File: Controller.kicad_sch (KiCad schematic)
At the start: 39 parts, among them J1 USB4105-GF-A-060, J2 SWD, SW61 BOOTSEL, SW62 RESET, U1 RP2354A, U2 AP2112K-3.3TRG1, U3 USBLC6-2SC6, X1 12MHz

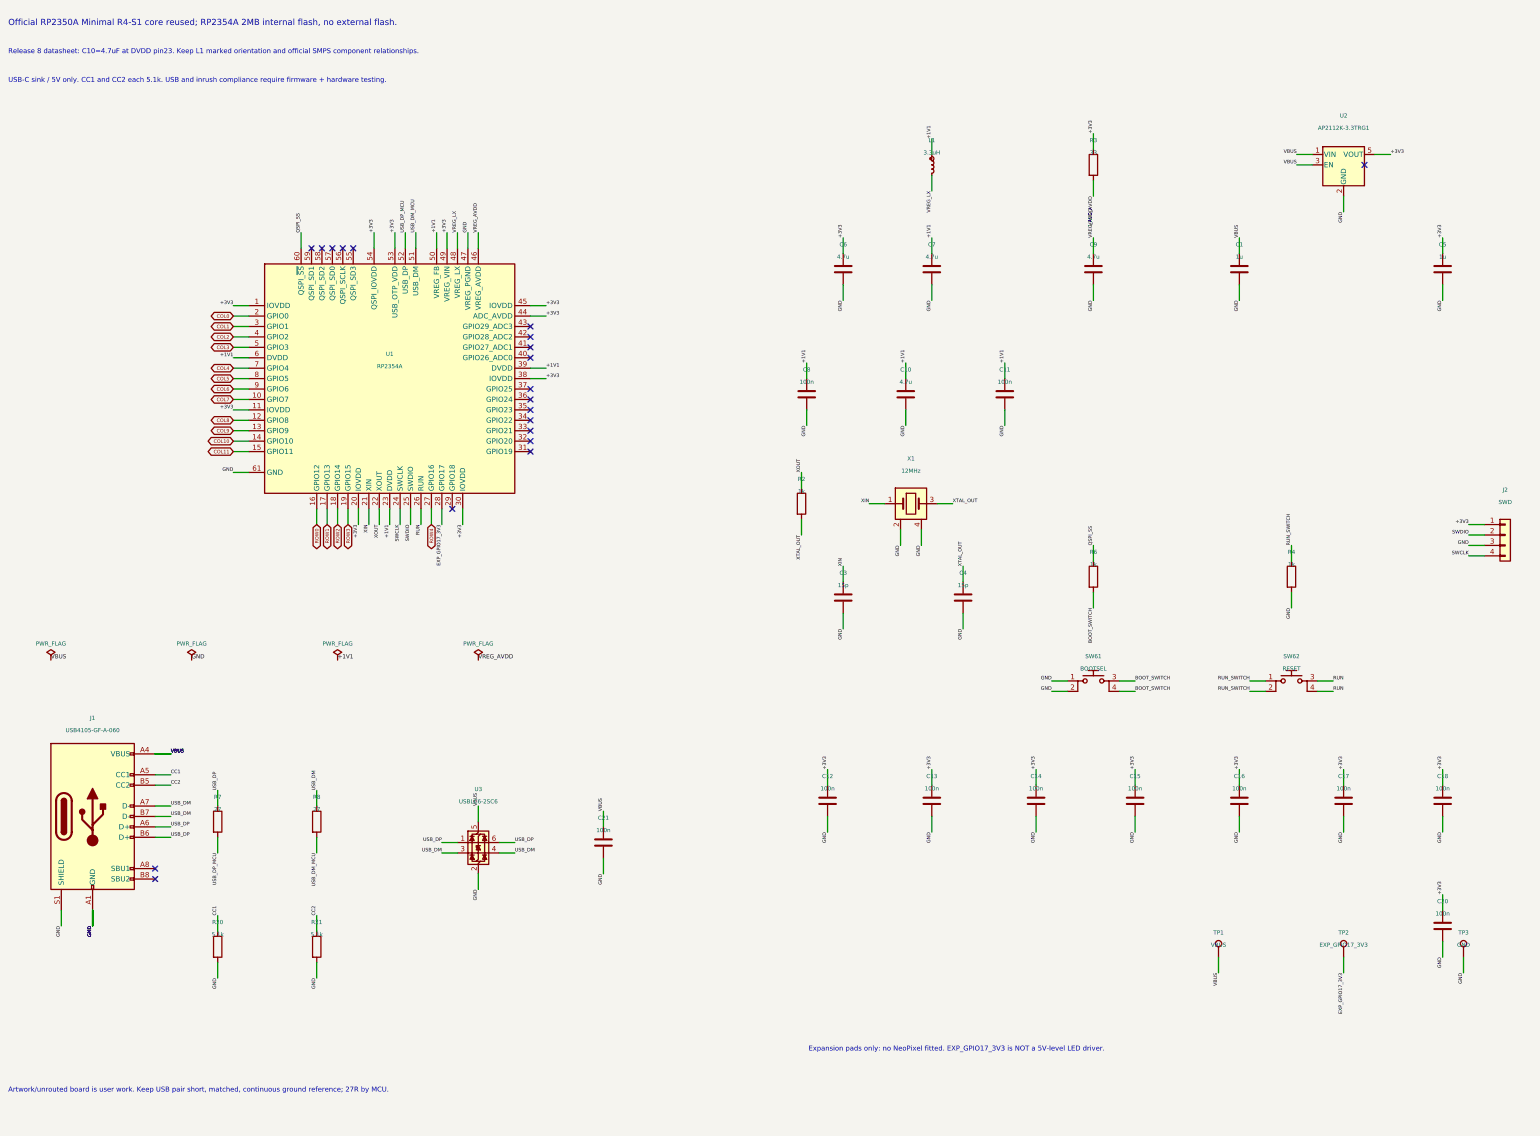
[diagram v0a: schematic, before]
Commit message: Refine WING27 schematics, SWD connector, panel overlay and mounting
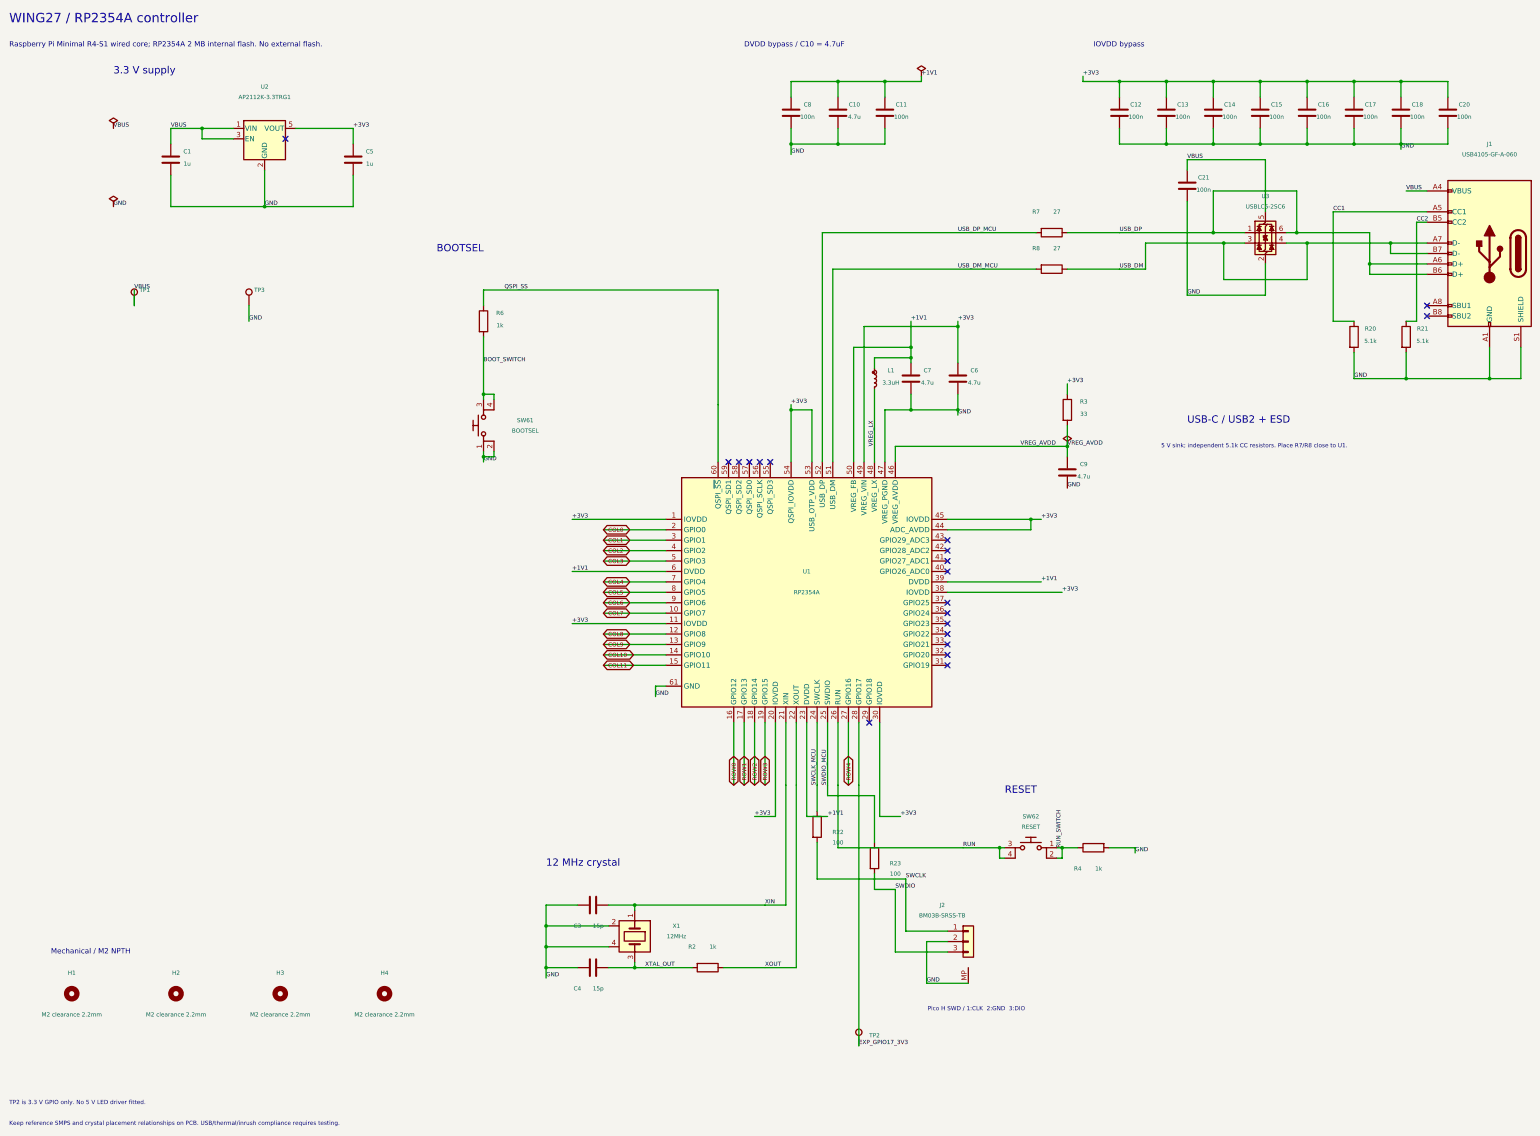
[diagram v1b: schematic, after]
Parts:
- added H1, H2, H3, H4: M2 clearance 2.2mm, WING27:MountingHole_2.2mm_M2, symbol WING27:MountingHole
- added R22, R23: 100, WING27:RPI_generic_resc1005x35, symbol WING27:R
- J2: value SWD -> BM03B-SRSS-TB; footprint WING27:PinHeader_1x04_P1.27mm_Vertical -> WING27:JST_SH_BM03B-SRSS-TB_1x03-1MP_P1.00mm_Vertical; symbol WING27:Conn_01x04 -> WING27:Conn_01x03; LCSC (none) -> C5306067; manufacturer (none) -> JST; manufacturer_pn (none) -> BM03B-SRSS-TB(LF)(SN); now in the parts list
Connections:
- net +3V3: no longer J2.1 (Pin_1)
- net GND: now also J2.2 (Pin_2), J2.MP; no longer J2.3 (Pin_3)
- net SWCLK: now also J2.1 (Pin_1), R22.2; no longer J2.4 (Pin_4), U1.24 (SWCLK)
- net SWDIO: now also J2.3 (Pin_3), R23.2; no longer J2.2 (Pin_2), U1.25 (SWDIO)
- new net SWCLK_MCU: R22.1, U1.24 (SWCLK)
- new net SWDIO_MCU: R23.1, U1.25 (SWDIO)
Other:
- note added: "12 MHz crystal"
- note added: "3.3 V supply"
- note added: "5 V sink; independent 5.1k CC resistors. Place R7/R8 close to U1."
- note added: "BOOTSEL"
- note added: "DVDD bypass / C10 = 4.7uF"
- note added: "IOVDD bypass"
- note added: "Keep reference SMPS and crystal placement relationships on PCB. USB/thermal/inrush compliance requires testing."
- note added: "Mechanical / M2 NPTH"
- note added: "Pico H SWD / 1:CLK 2:GND 3:DIO"
- note added: "RESET"
- note added: "Raspberry Pi Minimal R4-S1 wired core; RP2354A 2 MB internal flash. No external flash."
- note added: "TP2 is 3.3 V GPIO only. No 5 V LED driver fitted."
- note added: "USB-C / USB2 + ESD"
- note added: "WING27 / RP2354A controller"
- note removed: "Artwork/unrouted board is user work. Keep USB pair short, matched, continuous ground reference; 27R by MCU."
- note removed: "Expansion pads only: no NeoPixel fitted. EXP_GPIO17_3V3 is NOT a 5V-level LED driver."
- note removed: "Official RP2350A Minimal R4-S1 core reused; RP2354A 2MB internal flash, no external flash."
- note removed: "Release 8 datasheet: C10=4.7uF at DVDD pin23. Keep L1 marked orientation and official SMPS component relationships."
- note removed: "USB-C sink / 5V only. CC1 and CC2 each 5.1k. USB and inrush compliance require firmware + hardware testing."
- company: (none) -> ハシビロ工業
- moved on the sheet: C1, C10, C11, C12, C13, C14, C15, C16, C17, C18, C20, C21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

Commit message: Split keyboard GPIO banks and refine basic parts and SWD options
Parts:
- added J3: SWD 2.54 DNP, WING27:PinHeader_1x03_P2.54mm_Vertical, symbol WING27:SWD_TEST_3PIN
- C5: value 1u -> 4.7u; LCSC C15849 -> C19666; manufacturer_pn CL10A105KB8NNNC -> CL10A475KO8NNNC
- SW61, SW62: footprint WING27:RPI_wurthelek_434133025816 -> WING27:SW_SPST_TS-1088-AR02016; symbol WING27:BOOT_RUN_SW -> WING27:BOOT_RESET_2PIN; LCSC (none) -> C720477; manufacturer Wurth Elektronik -> XUNPU; manufacturer_pn 434133025816 -> TS-1088-AR02016
- U2: value AP2112K-3.3TRG1 -> XC6206P332MR-G; footprint WING27:SOT-23-5 -> WING27:XC6206_SOT23_Torex_Reference; symbol WING27:AP2112K-3.3 -> WING27:XC6206PxxxMR; LCSC C51118 -> C5446; manufacturer Diodes Incorporated -> Torex Semiconductor; manufacturer_pn AP2112K-3.3TRG1 -> XC6206P332MR-G
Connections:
- net +3V3: now also U2.2 (VO); no longer U2.5 (VOUT)
- net BOOT_SWITCH: now also SW61.2; no longer SW61.3, SW61.4
- net COL0: now also U1.31 (GPIO19); no longer U1.2 (GPIO0)
- net COL1: now also U1.32 (GPIO20); no longer U1.3 (GPIO1)
- net COL2: now also U1.33 (GPIO21); no longer U1.4 (GPIO2)
- net COL3: now also U1.34 (GPIO22); no longer U1.5 (GPIO3)
- net COL4: now also U1.35 (GPIO23); no longer U1.7 (GPIO4)
- net COL5: now also U1.36 (GPIO24); no longer U1.8 (GPIO5)
- net GND: now also U2.1 (GND), J3.2 (Pin_2); no longer SW61.2, U2.2 (GND)
- net RUN: now also SW62.2; no longer SW62.3, SW62.4
- net RUN_SWITCH: no longer SW62.2
- net SWCLK: now also J3.1 (Pin_1)
- net SWDIO: now also J3.3 (Pin_3)
- net VBUS: no longer U2.1 (VIN)
- net ROW_L0: now reaches U1.37 (GPIO25)
- net ROW_L1: now reaches U1.40 (GPIO26_ADC0)
- net ROW_L2: now reaches U1.41 (GPIO27_ADC1)
- net ROW_L3: now reaches U1.42 (GPIO28_ADC2)
- net ROW_L4: now reaches U1.43 (GPIO29_ADC3)
- net ROW0: no longer names the net of U1.16 (GPIO12)
- net ROW1: no longer names the net of U1.17 (GPIO13)
- net ROW2: no longer names the net of U1.18 (GPIO14)
- net ROW3: no longer names the net of U1.19 (GPIO15)
- net ROW4: no longer names the net of U1.27 (GPIO16)
- new net ROW_R0: U1.2 (GPIO0)
- new net ROW_R1: U1.3 (GPIO1)
- new net ROW_R2: U1.4 (GPIO2)
- new net ROW_R3: U1.5 (GPIO3)
- new net ROW_R4: U1.7 (GPIO4)
- no-connect marks 20 -> 14

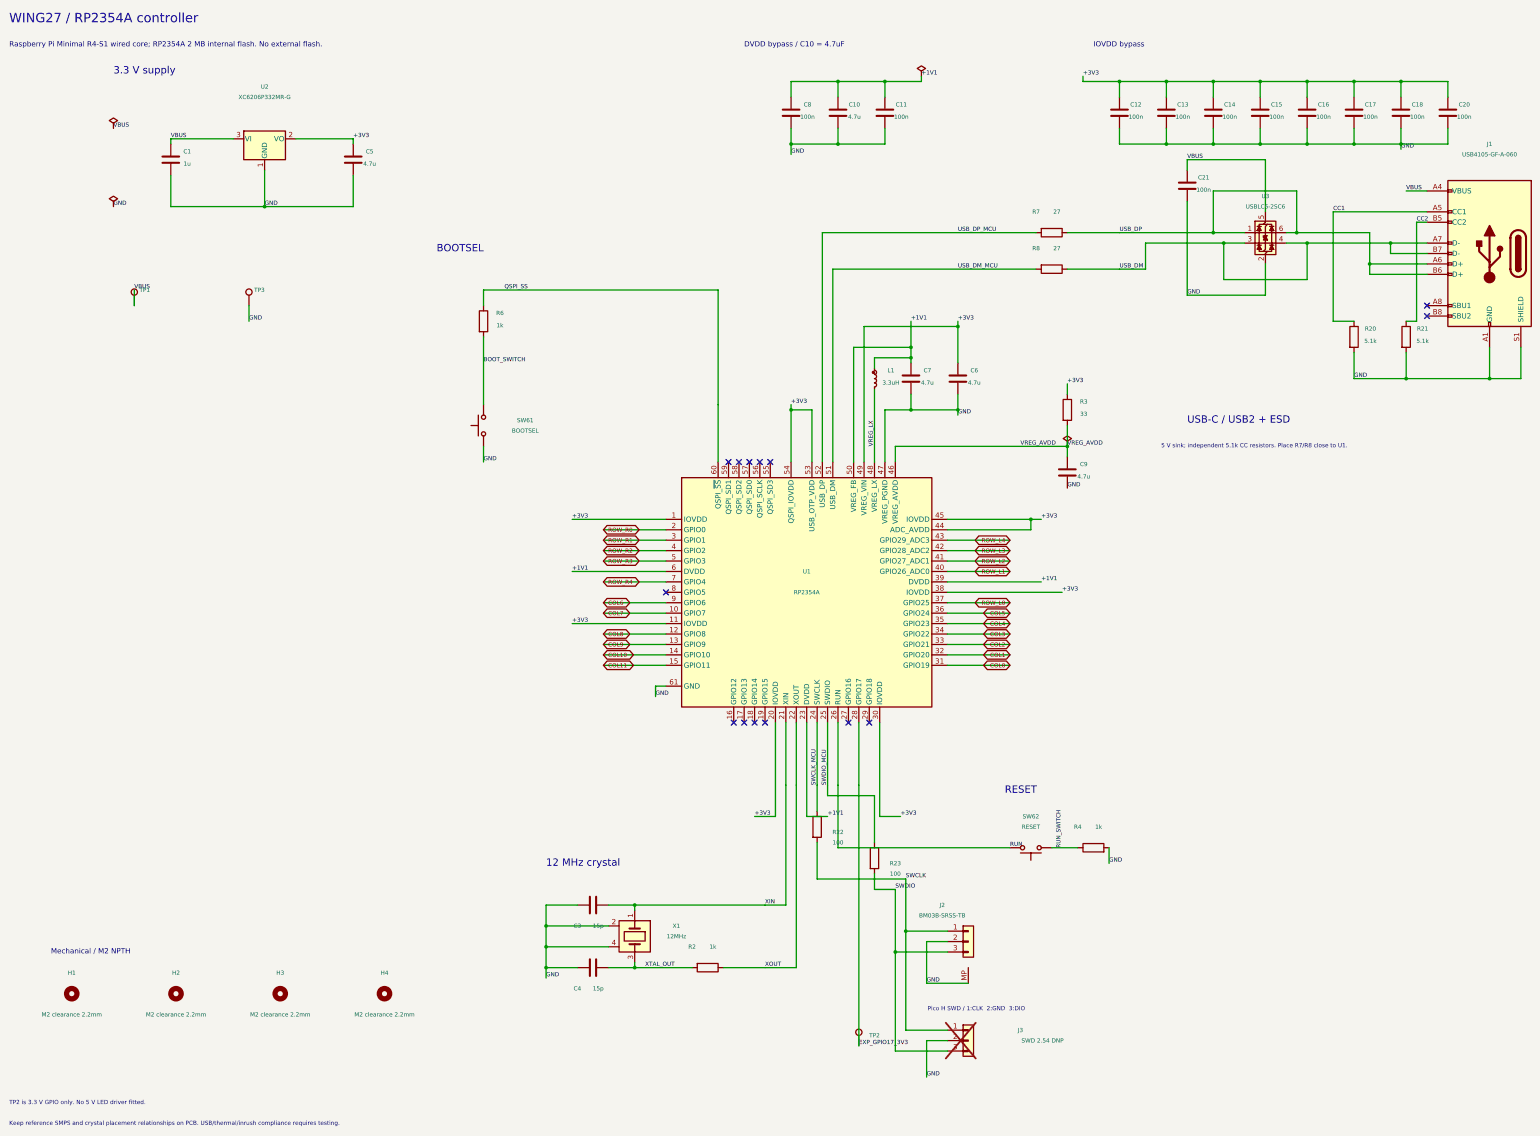
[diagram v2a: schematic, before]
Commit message: Arrange controller schematic from USB and power to MCU
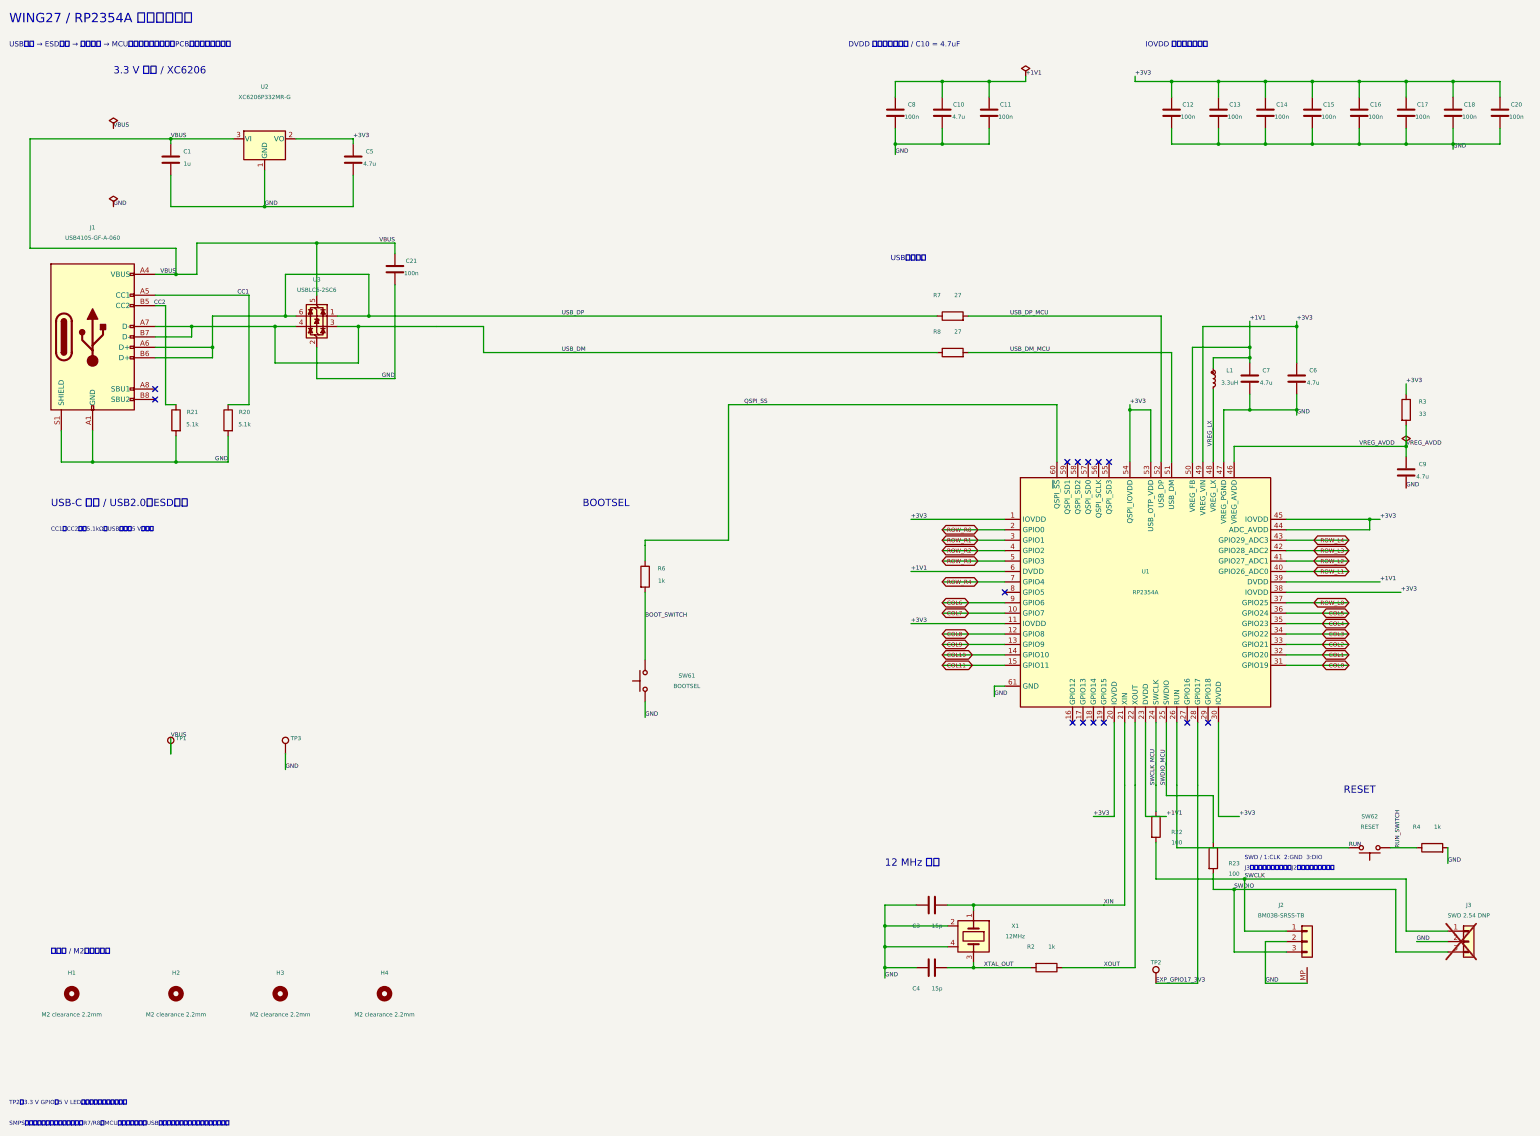
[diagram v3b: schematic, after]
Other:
- note added: "12 MHz 水晶"
- note added: "3.3 V 電源 / XC6206"
- note added: "CC1・CC2は各5.1kΩ。USB給電は5 Vのみ。"
- note added: "DVDD デカップリング / C10 = 4.7uF"
- note added: "IOVDD デカップリング"
- note added: "J3は未実装の代替端子。J2と同時接続しない。"
- note added: "SMPS・水晶は公式配置関係を維持。R7/R8はMCUの近くに配置。USB・発熱・突入電流は実機検証が必要。"
- note added: "SWD / 1:CLK 2:GND 3:DIO"
- note added: "TP2は3.3 V GPIO。5 V LEDドライバは搭載しない。"
- note added: "USB-C 入力 / USB2.0・ESD保護"
- note added: "USB入力 → ESD保護 → 直列抵抗 → MCU。電気接続・部品・PCB配置は変更なし。"
- note added: "USB直列抵抗"
- note added: "WING27 / RP2354A コントローラ"
- note added: "取付穴 / M2・非めっき"
- note removed: "12 MHz crystal"
- note removed: "3.3 V supply"
- note removed: "5 V sink; independent 5.1k CC resistors. Place R7/R8 close to U1."
- note removed: "DVDD bypass / C10 = 4.7uF"
- note removed: "IOVDD bypass"
- note removed: "Keep reference SMPS and crystal placement relationships on PCB. USB/thermal/inrush compliance requires testing."
- note removed: "Mechanical / M2 NPTH"
- note removed: "Pico H SWD / 1:CLK 2:GND 3:DIO"
- note removed: "Raspberry Pi Minimal R4-S1 wired core; RP2354A 2 MB internal flash. No external flash."
- note removed: "TP2 is 3.3 V GPIO only. No 5 V LED driver fitted."
- note removed: "USB-C / USB2 + ESD"
- note removed: "WING27 / RP2354A controller"
- moved on the sheet: C10, C11, C12, C13, C14, C15, C16, C17, C18, C20, C21, C3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
